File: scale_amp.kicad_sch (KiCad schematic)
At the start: 7 parts

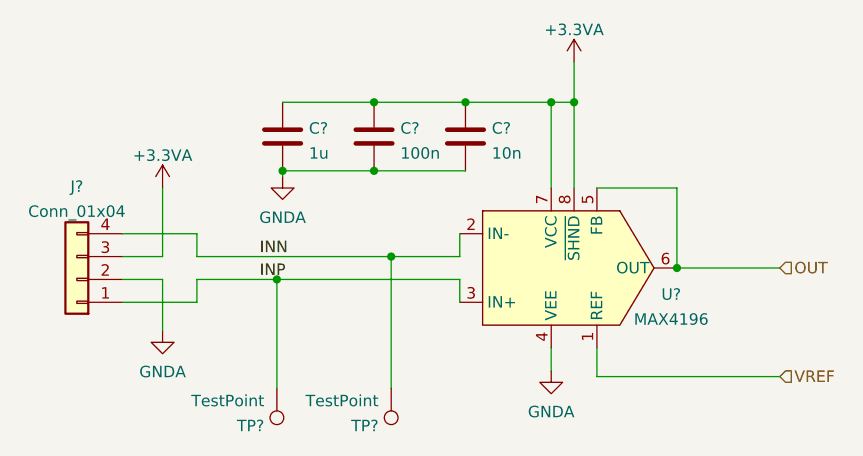
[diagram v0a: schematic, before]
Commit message: some form of schematic done, still lots to test
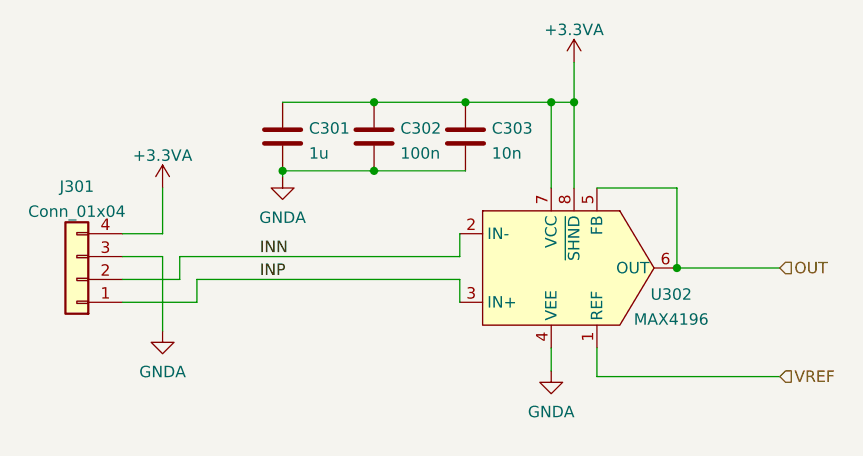
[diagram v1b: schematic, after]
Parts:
- removed TP? (x2): TestPoint, TestPoint:TestPoint_Pad_1.0x1.0mm, symbol Connector:TestPoint
- gave numbers to parts that had none: 5
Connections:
- net +3.3VA: now also J301.4 (Pin_4); no longer J301.3 (Pin_3)
- net GNDA: now also J301.3 (Pin_3); no longer J301.2 (Pin_2)
- net INN: now also J301.2 (Pin_2); no longer J301.4 (Pin_4)
